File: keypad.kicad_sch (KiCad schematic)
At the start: 10 parts, among them SW1 SW_Push, SW2 SW_Push, SW3 SW_Push, SW4 SW_Push, SW5 SW_Push, SW6 SW_Push, SW7 SW_Push, SW8 SW_Push, SW9 SW_Push, U1 ESP32-S3-DevKitC-1

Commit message: start pbc
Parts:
- SW1, SW2, SW3, SW4, SW5, SW6, SW7, SW8, SW9: footprint (none) -> Button_Switch_THT:SW_PUSH-12mm
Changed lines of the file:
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@@
 			)
 		)
-		(property "Footprint" ""
+		(property "Footprint" "Button_Switch_THT:SW_PUSH-12mm"
 			(at 148.59 71.12 0)
 			(hide yes)
@@
 			)
 		)
-		(property "Footprint" ""
+		(property "Footprint" "Button_Switch_THT:SW_PUSH-12mm"
 			(at 148.59 82.55 0)
 			(hide yes)
@@
 			)
 		)
-		(property "Footprint" ""
+		(property "Footprint" "Button_Switch_THT:SW_PUSH-12mm"
 			(at 163.83 59.69 0)
 			(hide yes)
@@
 			)
 		)
-		(property "Footprint" ""
+		(property "Footprint" "Button_Switch_THT:SW_PUSH-12mm"
 			(at 132.08 82.55 0)
 			(hide yes)
@@
 			)
 		)
-		(property "Footprint" ""
+		(property "Footprint" "Button_Switch_THT:SW_PUSH-12mm"
 			(at 163.83 71.12 0)
 			(hide yes)
@@
 			)
 		)
-		(property "Footprint" ""
+		(property "Footprint" "Button_Switch_THT:SW_PUSH-12mm"
 			(at 163.83 82.55 0)
 			(hide yes)
@@
 			)
 		)
-		(property "Footprint" ""
+		(property "Footprint" "Button_Switch_THT:SW_PUSH-12mm"
 			(at 148.59 59.69 0)
 			(hide yes)
@@
 			)
 		)
-		(property "Footprint" ""
+		(property "Footprint" "Button_Switch_THT:SW_PUSH-12mm"
 			(at 132.08 59.69 0)
 			(hide yes)
@@
 			)
 		)
-		(property "Footprint" ""
+		(property "Footprint" "Button_Switch_THT:SW_PUSH-12mm"
 			(at 132.08 71.12 0)
 			(hide yes)

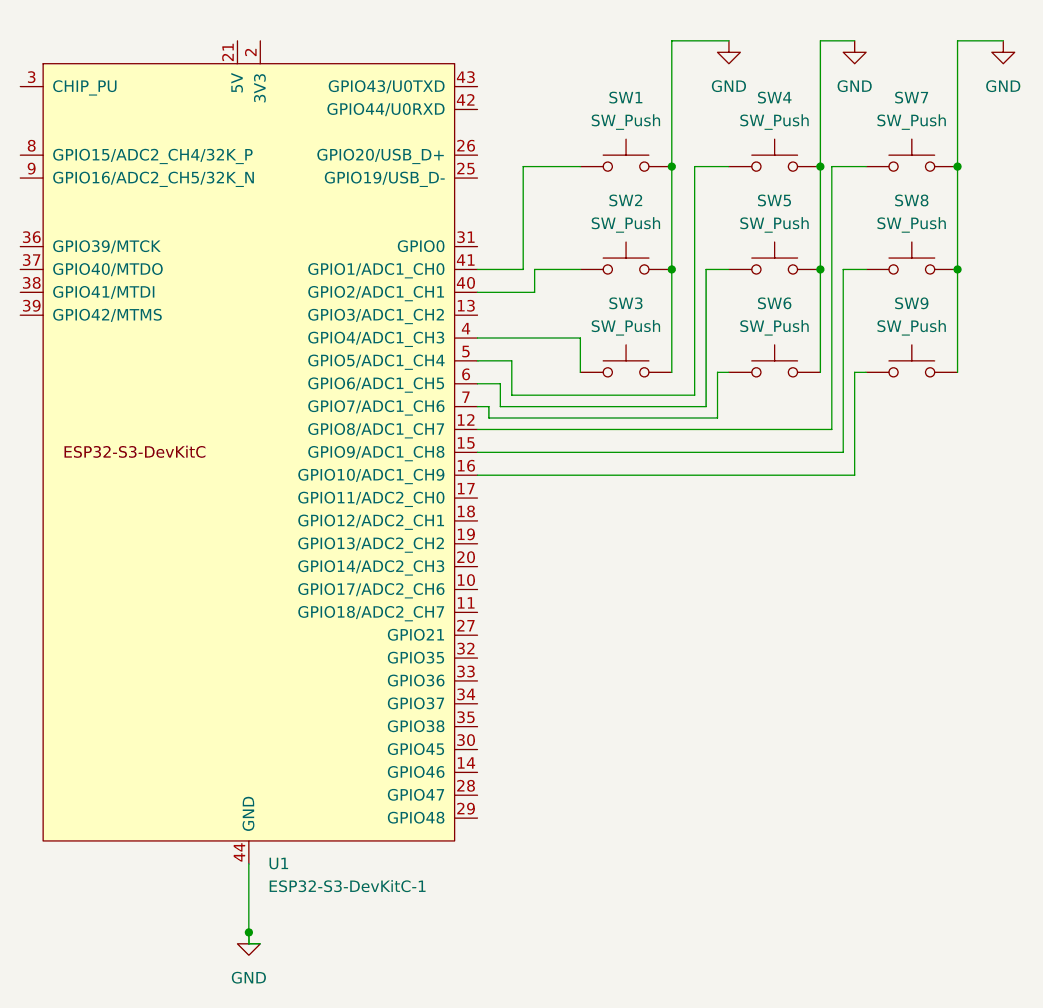
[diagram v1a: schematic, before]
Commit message: move connections
I moved all the connections so that they make more sense on the pbc.
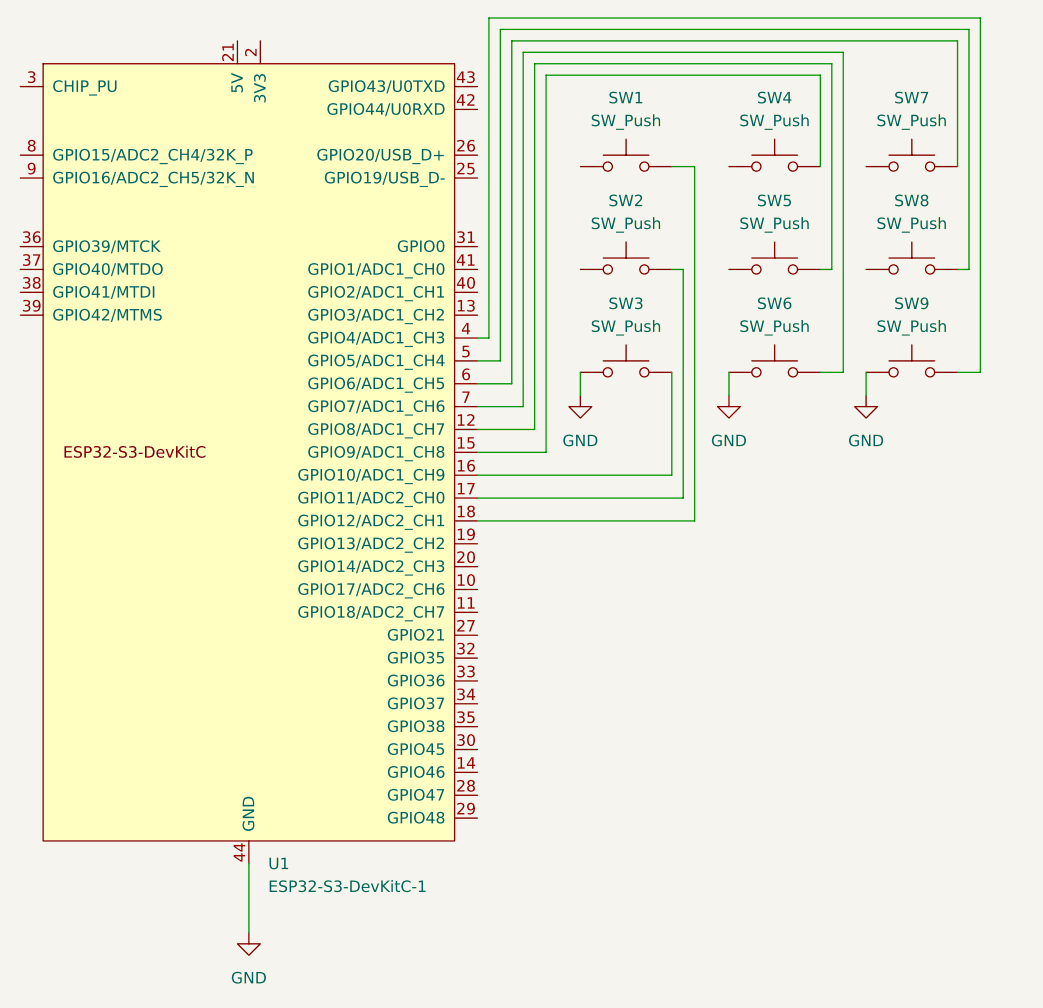
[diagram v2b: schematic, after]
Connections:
- net GND: now also SW3.1, SW6.1, SW9.1; no longer SW1.2, SW2.2, SW3.2, SW4.2, SW5.2, SW6.2, SW7.2, SW8.2, SW9.2
- net at SW5.1: no longer U1.6 (GPIO6/ADC1_CH5)
- net at U1.12 (GPIO8/ADC1_CH7): now also SW5.2; no longer SW7.1
- net at U1.15 (GPIO9/ADC1_CH8): now also SW4.2; no longer SW8.1
- net at U1.16 (GPIO10/ADC1_CH9): now also SW3.2; no longer SW9.1
- net at U1.17 (GPIO11/ADC2_CH0): now also SW2.2
- net at U1.18 (GPIO12/ADC2_CH1): now also SW1.2
- net at U1.4 (GPIO4/ADC1_CH3): now also SW9.2; no longer SW3.1
- net at U1.40 (GPIO2/ADC1_CH1): no longer SW2.1
- net at U1.41 (GPIO1/ADC1_CH0): no longer SW1.1
- net at U1.5 (GPIO5/ADC1_CH4): now also SW8.2; no longer SW4.1
- net at U1.7 (GPIO7/ADC1_CH6): now also SW6.2; no longer SW6.1
- new net: SW7.2, U1.6 (GPIO6/ADC1_CH5)

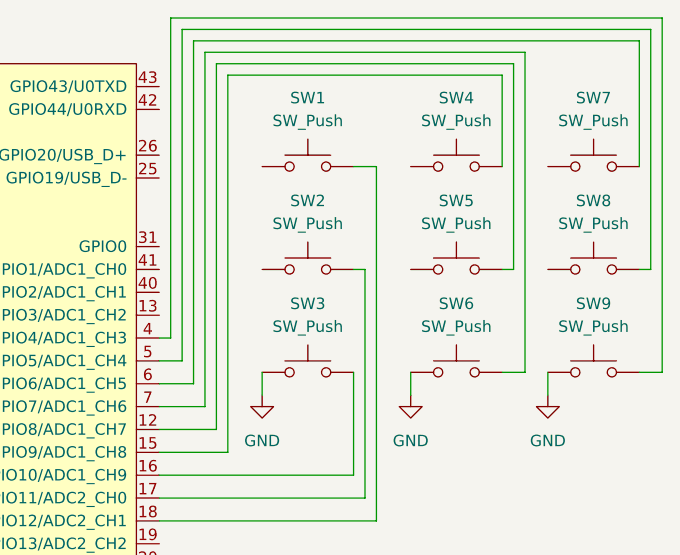
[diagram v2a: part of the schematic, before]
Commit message: fix grounding on schematic
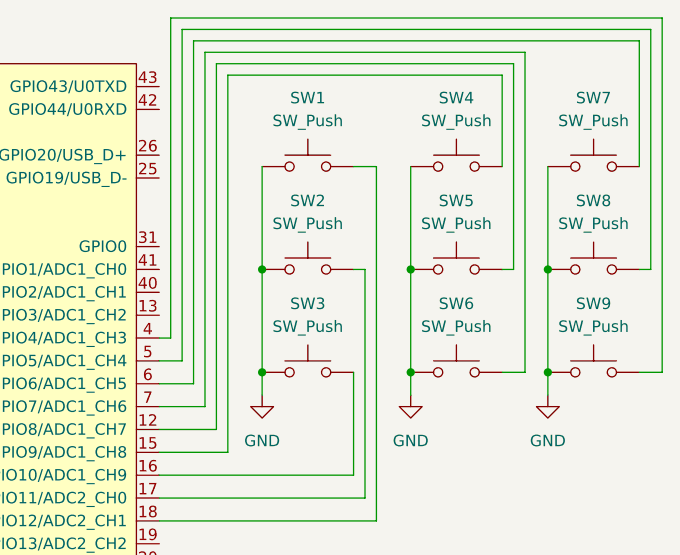
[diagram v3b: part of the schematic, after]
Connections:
- net GND: now also SW1.1, SW2.1, SW4.1, SW5.1, SW7.1, SW8.1
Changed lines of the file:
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@@
 	(generator_version "10.0")
 	(paper "A4")
+	(junction
+		(at 158.75 76.2)
+		(diameter 0)
+		(color 0 0 0 0)
+	)
+	(junction
+		(at 143.51 76.2)
+		(diameter 0)
+		(color 0 0 0 0)
+	)
+	(junction
+		(at 127 76.2)
+		(diameter 0)
+		(color 0 0 0 0)
+	)
+	(junction
+		(at 158.75 87.63)
+		(diameter 0)
+		(color 0 0 0 0)
+	)
+	(junction
+		(at 127 87.63)
+		(diameter 0)
+		(color 0 0 0 0)
+	)
+	(junction
+		(at 143.51 87.63)
+		(diameter 0)
+		(color 0 0 0 0)
+	)
 	(wire
 		(pts
@@
 	(wire
 		(pts
+			(xy 127 76.2) (xy 127 87.63)
+		)
+		(stroke
+			(width 0)
+			(type default)
+		)
+	)
+	(wire
+		(pts
 			(xy 168.91 64.77) (xy 168.91 50.8)
 		)
@@
 	(wire
 		(pts
+			(xy 143.51 64.77) (xy 143.51 76.2)
+		)
+		(stroke
+			(width 0)
+			(type default)
+		)
+	)
+	(wire
+		(pts
 			(xy 127 87.63) (xy 127 90.17)
 		)
@@
 	(wire
 		(pts
+			(xy 143.51 76.2) (xy 143.51 87.63)
+		)
+		(stroke
+			(width 0)
+			(type default)
+		)
+	)
+	(wire
+		(pts
 			(xy 120.65 91.44) (xy 115.57 91.44)
 		)
@@
 	(wire
 		(pts
+			(xy 158.75 64.77) (xy 158.75 76.2)
+		)
+		(stroke
+			(width 0)
+			(type default)
+		)
+	)
+	(wire
+		(pts
 			(xy 170.18 76.2) (xy 170.18 49.53)
 		)
@@
 	(wire
 		(pts
+			(xy 127 64.77) (xy 127 76.2)
+		)
+		(stroke
+			(width 0)
+			(type default)
+		)
+	)
+	(wire
+		(pts
 			(xy 168.91 50.8) (xy 119.38 50.8)
 		)
 		(stroke
+			(width 0)
+			(type default)
+		)
+	)
+	(wire
+		(pts
+			(xy 158.75 76.2) (xy 158.75 87.63)
+		)
+		(stroke
